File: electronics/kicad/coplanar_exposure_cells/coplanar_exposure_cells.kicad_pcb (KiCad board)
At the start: 2 copper layers, 10 parts

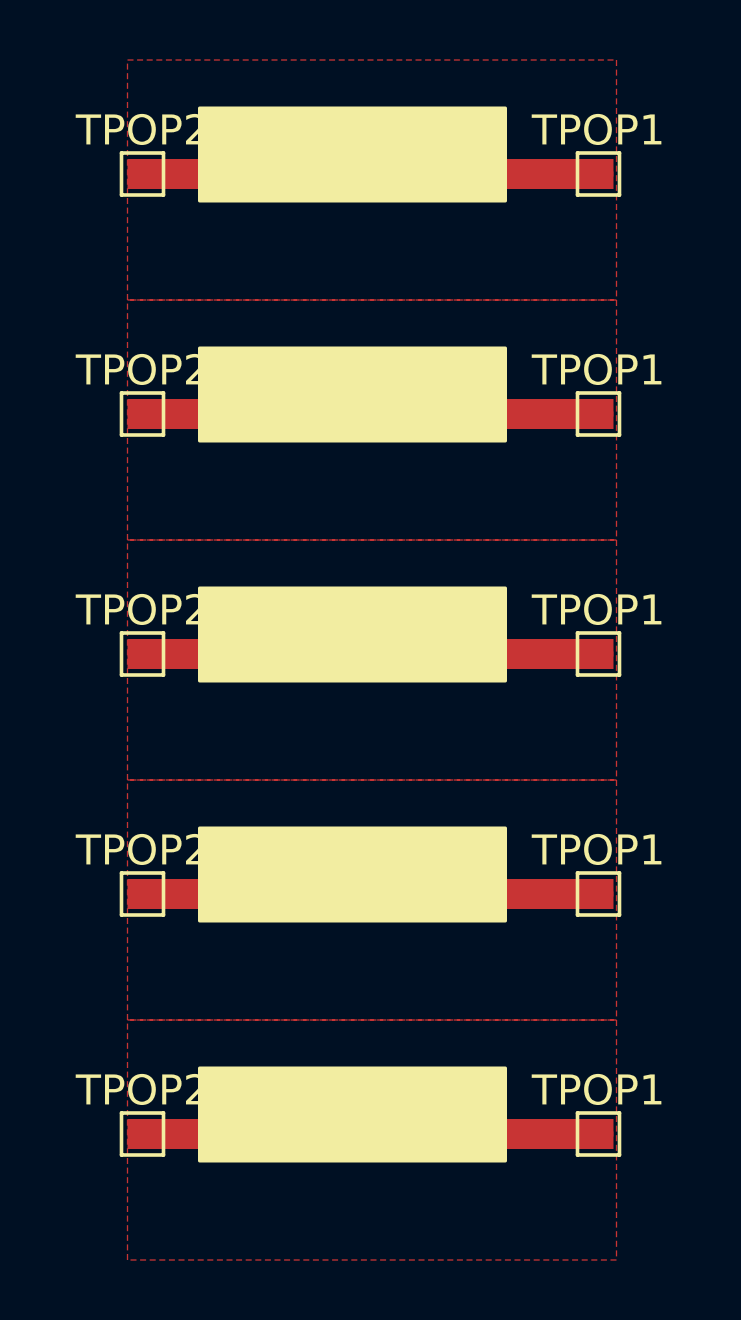
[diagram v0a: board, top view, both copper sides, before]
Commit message: all data is questionable; autosampler was right fucked fuck fuck fuck fuck fuck fuck fuck fuck fuck fuck fuck fuck fuck fuck fuck fuck fuck fuck
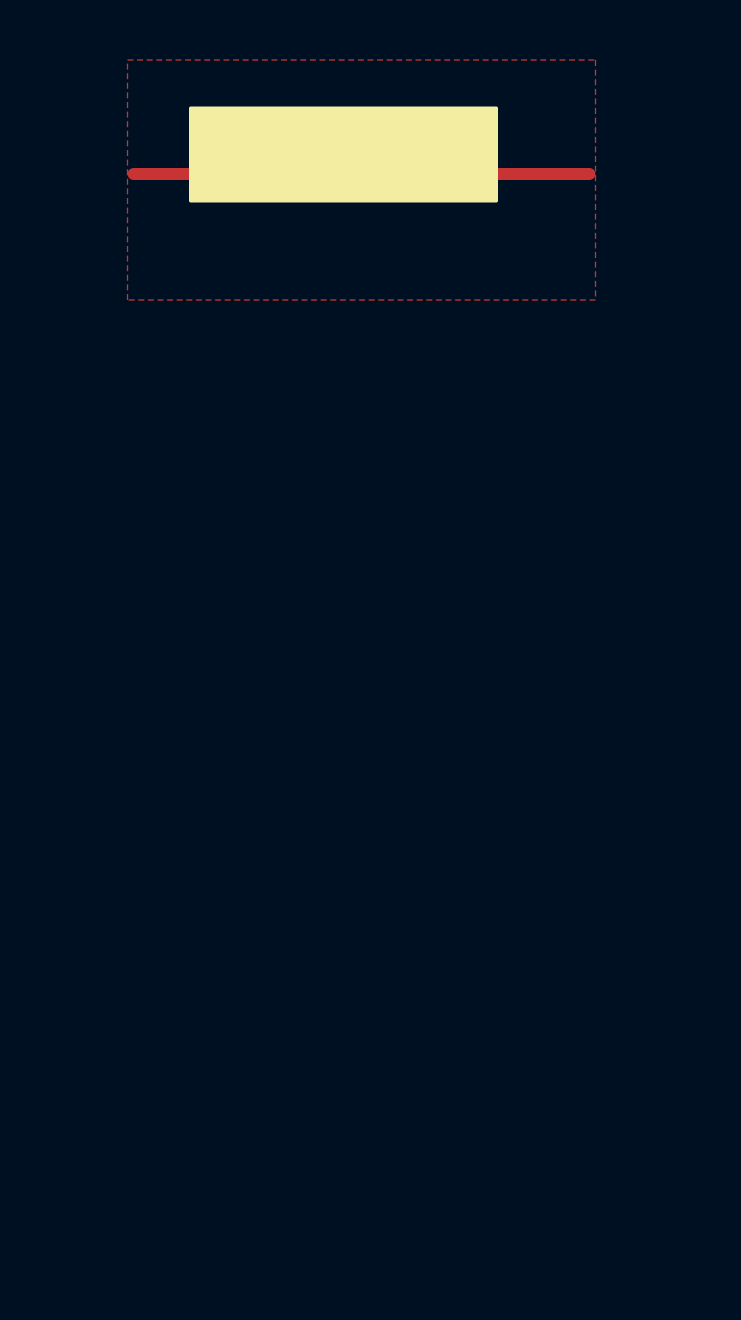
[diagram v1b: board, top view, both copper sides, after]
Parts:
- removed TPOP1 (x5), TPOP2 (x5): Voutput, TestPoint:TestPoint_Pad_1.0x1.0mm
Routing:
- net (no net): track 60.8 -> 0.00 mm
